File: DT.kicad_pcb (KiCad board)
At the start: 2 copper layers, 52 parts, among them SW1 SW_Push, SW10 SW_Push, SW11 SW_Push, SW12 SW_Push, SW2 SW_Push, SW3 SW_Push, SW4 SW_Push, SW5 SW_Push, SW6 SW_Push, SW7 SW_Push, SW8 SW_Push, SW9 SW_Push

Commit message: started wiring
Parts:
- removed REF**: DIP-28_W7.62mm, Package_DIP:DIP-28_W7.62mm
- removed REF**: Arduino_Nano, Module:Arduino_Nano
- added A1: Arduino_Nano_Every, Module:Arduino_Nano, F.Cu at (-260.8, 40.6)
- added R26: R, Resistor_THT:R_Axial_DIN0204_L3.6mm_D1.6mm_P5.08mm_Horizontal, F.Cu at (-241.6, 30.5)
- added U1: MCP23017_SP, Package_DIP:DIP-28_W7.62mm, F.Cu at (-253.8, -7.27)
- R1, R10, R11, R12, R13, R14, R15, R16, R17, R18, R19, R2, R20, R21, R22, R23, R24, R25, R3, R4, R5, R6, R7, R8, R9: footprint Resistor_THT:R_Axial_DIN0204_L3.6mm_D1.6mm_P1.90mm_Vertical -> Resistor_THT:R_Axial_DIN0204_L3.6mm_D1.6mm_P5.08mm_Horizontal
- moved R9 120.8 mm to (-365.2, 54.3)
- moved R1 119.9 mm to (-365.3, -5.25)
- moved R5 115.6 mm to (-365.0, 24.5)
- moved R25 96.7 mm to (-283.4, -43.7)
- moved R2 93.4 mm to (-335.6, -5.35)
- moved R10 90.4 mm to (-334.9, 54.2)
- moved R6 87.4 mm to (-335.5, 24.4)
- moved R21 81.1 mm to (-266.5, -26.9)
- moved R23 79.6 mm to (-266.5, -39.2)
- moved R24 78.1 mm to (-266.5, -34.4)
- moved R19 77.5 mm to (-266.5, -29.4)
- moved R17 73.9 mm to (-266.5, -31.9)
- moved R15 72.7 mm to (-266.5, -36.9)
- moved R3 69.4 mm to (-305.8, -5.14)
- moved R20 68.8 mm to (-266.5, -16.9)
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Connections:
- net +5V renamed Net-(A1-+5V)
- net GND renamed Net-(DS1-LED(-))
- R13 pad 1: Net-(A1-PadD22) -> Net-(U1-GPA3)
- R14 pad 1: Net-(A1-PadD23) -> Net-(U1-GPA2)
- R15 pad 1: Net-(A1-PadD24) -> Net-(U1-GPA1)
- R16 pad 1: Net-(A1-PadD25) -> Net-(U1-GPA0)
- R17 pad 1: Net-(A1-PadD26) -> Net-(U1-GPB7)
- R18 pad 1: Net-(A1-PadD32) -> Net-(U1-GPB1)
- R19 pad 1: Net-(A1-PadD30) -> Net-(U1-GPB3)
- R20 pad 1: Net-(A1-PadD29) -> Net-(U1-GPB4)
- R21 pad 1: Net-(A1-PadD28) -> Net-(U1-GPB5)
- R22 pad 1: Net-(A1-PadD27) -> Net-(U1-GPB6)
- R23 pad 1: Net-(A1-PadD33) -> Net-(U1-GPB0)
- R24 pad 1: Net-(A1-PadD31) -> Net-(U1-GPB2)
- SW1 pad 1: Net-(A1-PadD22) -> Net-(U1-GPB0)
- SW10 pad 1: Net-(A1-PadD31) -> Net-(U1-GPA1)
- SW11 pad 1: Net-(A1-PadD32) -> Net-(U1-GPA2)
- SW12 pad 1: Net-(A1-PadD33) -> Net-(U1-GPA3)
- SW2 pad 1: Net-(A1-PadD23) -> Net-(U1-GPB1)
- SW3 pad 1: Net-(A1-PadD24) -> Net-(U1-GPB2)
- SW4 pad 1: Net-(A1-PadD25) -> Net-(U1-GPB3)
- SW5 pad 1: Net-(A1-PadD26) -> Net-(U1-GPB4)
- SW6 pad 1: Net-(A1-PadD27) -> Net-(U1-GPB5)
- SW7 pad 1: Net-(A1-PadD28) -> Net-(U1-GPB6)
- SW8 pad 1: Net-(A1-PadD29) -> Net-(U1-GPB7)
- SW9 pad 1: Net-(A1-PadD30) -> Net-(U1-GPA0)
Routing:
- net Net-(DS1-LED(-)): track 0.00 -> 173.7 mm, vias 0 -> 1
- net Net-(A1-D5): track 0.00 -> 114.5 mm
- net Net-(A1-D7): track 0.00 -> 109.5 mm, vias 0 -> 1
- net Net-(A1-D4): track 0.00 -> 85.3 mm
- net Net-(A1-D3): track 0.00 -> 56.0 mm
- net Net-(A1-D6): track 0.00 -> 54.9 mm, vias 0 -> 1
- net Net-(A1-D2): track 0.00 -> 25.4 mm
- net Net-(D10-A): track 0.00 -> 5.56 mm
- net Net-(D8-A): track 0.00 -> 5.29 mm
- net Net-(D11-A): track 0.00 -> 5.17 mm
- net Net-(D7-A): track 0.00 -> 5.15 mm
- net Net-(D9-A): track 0.00 -> 5.04 mm
- net Net-(D12-A): track 0.00 -> 4.26 mm

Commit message: more wiring
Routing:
- net Net-(A1-D9): track 0.00 -> 161.4 mm, vias 0 -> 1
- net Net-(DS1-LED(-)): track 173.7 -> 334.2 mm, vias 1 -> 3
- net Net-(A1-A1): track 0.00 -> 156.4 mm, vias 0 -> 3
- net Net-(A1-A0): track 0.00 -> 132.3 mm, vias 0 -> 2
- net Net-(A1-A2): track 0.00 -> 124.1 mm, vias 0 -> 2
- net Net-(A1-D8): track 0.00 -> 117.6 mm, vias 0 -> 4
- net Net-(A1-D10): track 0.00 -> 88.7 mm, vias 0 -> 2
- net Net-(D5-A): track 0.00 -> 5.22 mm
- net Net-(D3-A): track 0.00 -> 5.00 mm
- net Net-(D6-A): track 0.00 -> 4.97 mm
- net Net-(D2-A): track 0.00 -> 4.90 mm
- net Net-(D4-A): track 0.00 -> 4.87 mm

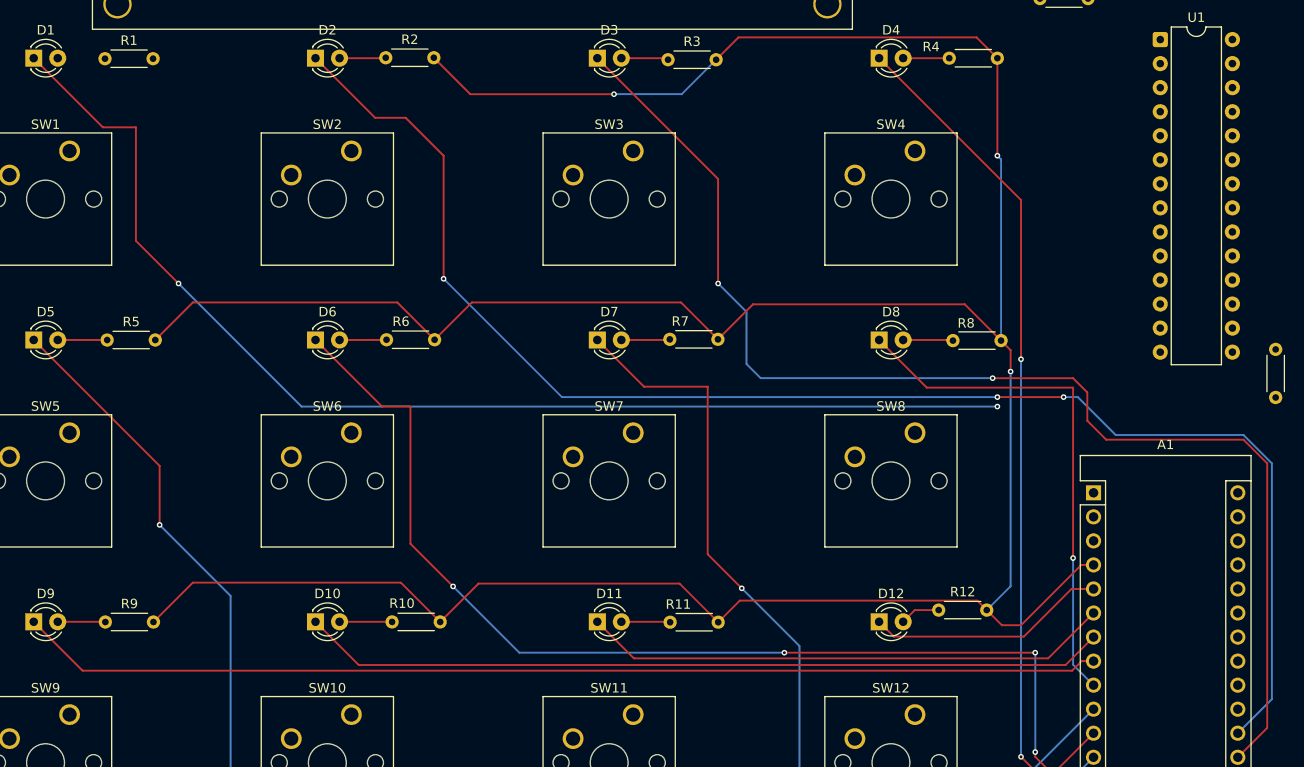
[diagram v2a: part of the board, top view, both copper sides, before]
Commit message: finished wiring LEDs
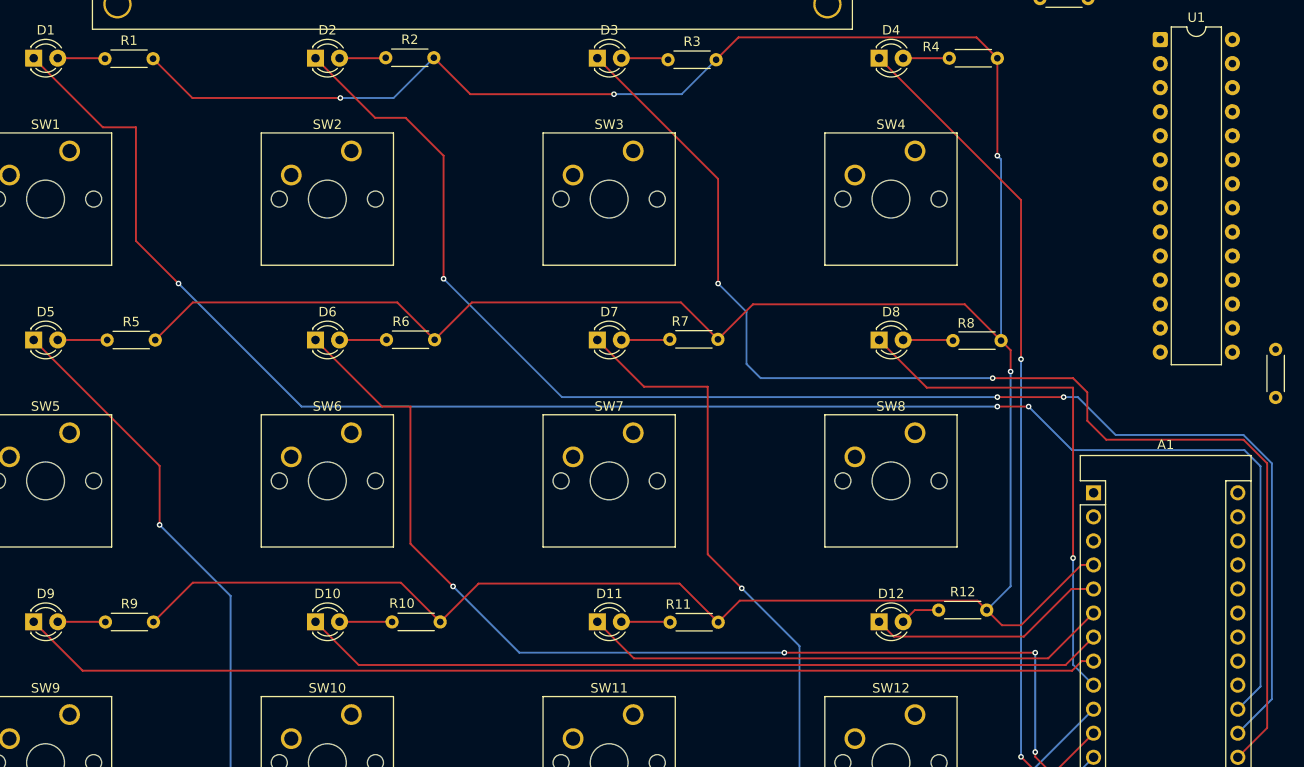
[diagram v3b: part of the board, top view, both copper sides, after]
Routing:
- net Net-(A1-A2): track 124.1 -> 181.2 mm, vias 2 -> 3
- net Net-(DS1-LED(-)): track 334.2 -> 367.4 mm, vias 3 -> 4
- net Net-(D1-A): track 0.00 -> 5.01 mm
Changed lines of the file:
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@@
+	)
+	(segment
+		(start -370.262 -5.305)
+		(end -365.325 -5.305)
+		(width 0.2)
+		(layer "F.Cu")
+		(net 1)
+	)
+	(segment
+		(start -365.325 -5.305)
+		(end -365.27 -5.25)
+		(width 0.2)
+		(layer "F.Cu")
+		(net 1)
 	)
 	(segment
@@
 	)
 	(segment
+		(start -271 31.5)
+		(end -267.7 31.5)
+		(width 0.2)
+		(layer "F.Cu")
+		(net 22)
+	)
+	(segment
 		(start -362 14)
 		(end -357.5 18.5)
@@
 	)
 	(via
+		(at -267.7 31.5)
+		(size 0.6)
+		(drill 0.3)
+		(layers "F.Cu" "B.Cu")
+		(net 22)
+	)
+	(via
 		(at -357.5 18.5)
 		(size 0.6)
@@
 		(drill 0.3)
 		(layers "F.Cu" "B.Cu")
+		(net 22)
+	)
+	(segment
+		(start -267.7 31.5)
+		(end -263.1 36.1)
+		(width 0.2)
+		(layer "B.Cu")
 		(net 22)
 	)
@@
 	)
 	(segment
+		(start -243.2 61.07)
+		(end -245.6 63.47)
+		(width 0.2)
+		(layer "B.Cu")
+		(net 22)
+	)
+	(segment
+		(start -243.2 37.8)
+		(end -243.2 61.07)
+		(width 0.2)
+		(layer "B.Cu")
+		(net 22)
+	)
+	(segment
+		(start -244.9 36.1)
+		(end -243.2 37.8)
+		(width 0.2)
+		(layer "B.Cu")
+		(net 22)
+	)
+	(segment
+		(start -263.1 36.1)
+		(end -244.9 36.1)
+		(width 0.2)
+		(layer "B.Cu")
+		(net 22)
+	)
+	(segment
 		(start -344.5 31.5)
 		(end -271 31.5)
@@
 	)
 	(segment
+		(start -360.19 -5.25)
+		(end -356.04 -1.1)
+		(width 0.2)
+		(layer "F.Cu")
+		(net 38)
+	)
+	(segment
+		(start -356.04 -1.1)
+		(end -340.4 -1.1)
+		(width 0.2)
+		(layer "F.Cu")
+		(net 38)
+	)
+	(segment
 		(start -304.57 50.2)
 		(end -300.49 54.28)
@@
 	)
 	(via
+		(at -340.4 -1.1)
+		(size 0.6)
+		(drill 0.3)
+		(layers "F.Cu" "B.Cu")
+		(net 38)
+	)
+	(via
 		(at -311.5 -1.5)
 		(size 0.6)
@@
 	)
 	(segment
+		(start -340.4 -1.1)
+		(end -334.78 -1.1)
+		(width 0.2)
+		(layer "B.Cu")
+		(net 38)
+	)
+	(segment
 		(start -271 5)
 		(end -270.61 5.39)
@@
 		(width 0.2)
 		(layer "B.Cu")
+		(net 38)
+	)
+	(segment
+		(start -334.78 -1.1)
+		(end -330.53 -5.35)
+		(width 0.2)
+		(layer "B.Cu")

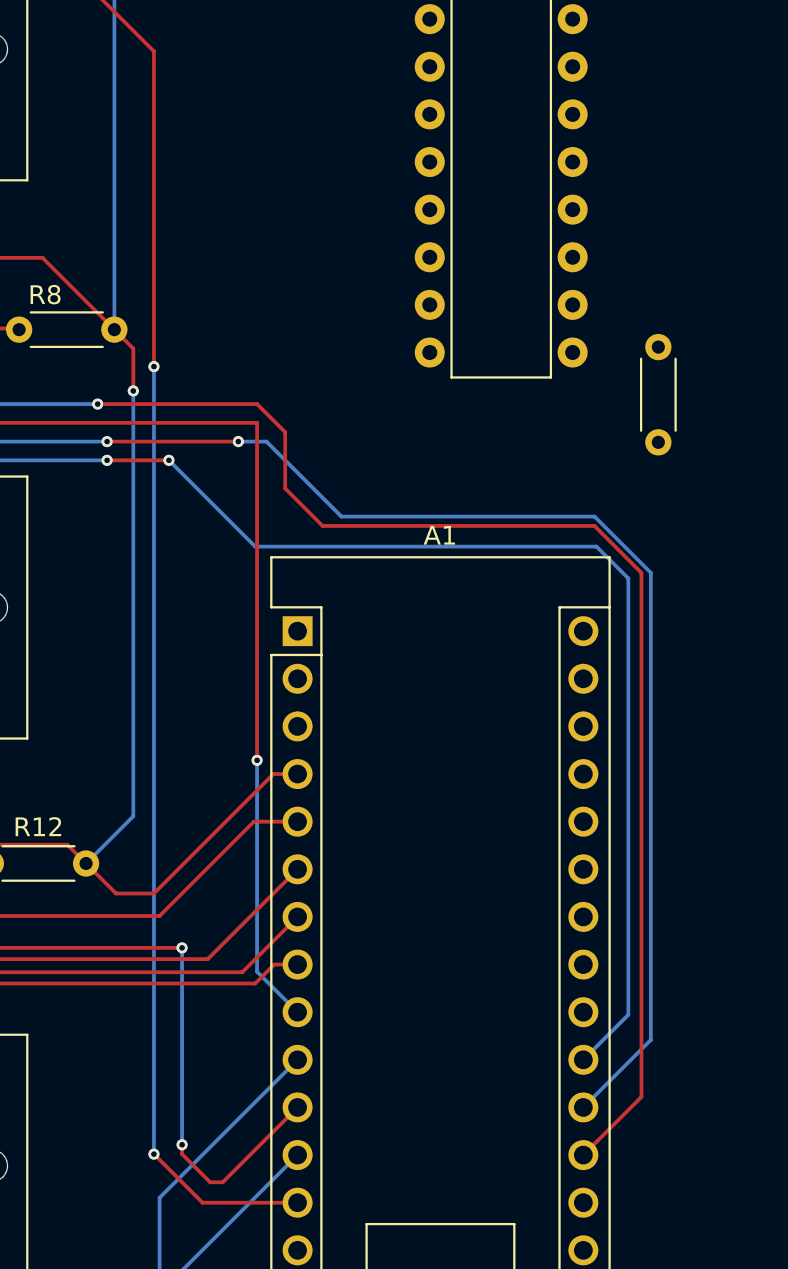
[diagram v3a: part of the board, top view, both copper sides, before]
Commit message: wired up mcp
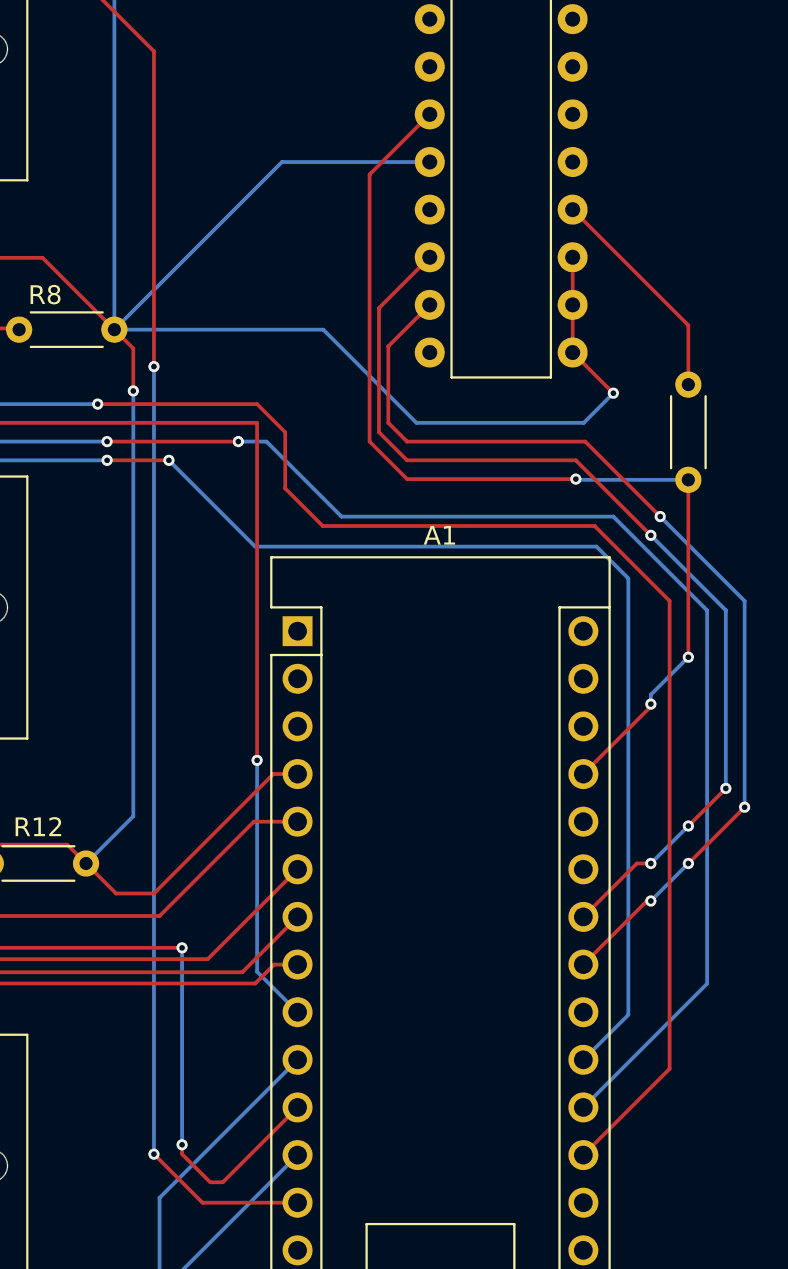
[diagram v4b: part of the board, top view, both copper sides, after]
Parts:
- moved R26 2.56 mm to (-240.0, 32.5)
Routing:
- net Net-(DS1-LED(-)): track 367.4 -> 425.4 mm, vias 4 -> 5
- net Net-(A1-+5V): track 0.00 -> 54.6 mm, vias 0 -> 3
- net Net-(A1-SDA/A4): track 0.00 -> 53.2 mm, vias 0 -> 4
- net Net-(A1-SCL/A5): track 0.00 -> 52.8 mm, vias 0 -> 4
- net Net-(U1-~{RESET}): track 0.00 -> 11.9 mm
- net Net-(A1-A1): track 156.4 -> 159.4 mm
- net Net-(A1-A0): track 132.3 -> 133.5 mm

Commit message: wirws
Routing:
- net Net-(U1-GPA0): track 0.00 -> 186.3 mm, vias 0 -> 3
- net Net-(U1-GPA1): track 0.00 -> 154.2 mm, vias 0 -> 3
- net Net-(U1-GPB4): track 0.00 -> 137.1 mm, vias 0 -> 4
- net Net-(U1-GPB0): track 0.00 -> 120.7 mm
- net Net-(U1-GPB5): track 0.00 -> 115.3 mm, vias 0 -> 3
- net Net-(U1-GPB1): track 0.00 -> 91.6 mm
- net Net-(U1-GPB6): track 0.00 -> 76.4 mm, vias 0 -> 5
- net Net-(U1-GPB2): track 0.00 -> 59.9 mm
- net Net-(U1-GPB7): track 0.00 -> 45.2 mm, vias 0 -> 1
- net Net-(U1-GPB3): track 0.00 -> 29.2 mm

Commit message: almost finished switches
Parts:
- moved R13 14.2 mm to (-252.3, -14.7)
- moved R14 14.2 mm to (-252.3, -11.9)
- moved R15 14.2 mm to (-252.3, -37.2)
- moved R16 14.2 mm to (-252.3, -22.2)
- moved R17 14.2 mm to (-252.3, -32.2)
- moved R18 14.2 mm to (-252.3, -19.8)
- moved R19 14.2 mm to (-252.3, -29.8)
- moved R20 14.2 mm to (-252.3, -17.2)
- moved R21 14.2 mm to (-252.3, -27.2)
- moved R22 14.2 mm to (-252.3, -24.8)
- moved R23 14.2 mm to (-252.3, -39.6)
- moved R24 14.2 mm to (-252.3, -34.8)
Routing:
- net Net-(A1-+5V): track 54.6 -> 491.7 mm, vias 3 -> 12
- net Net-(U1-GPA2): track 0.00 -> 165.4 mm, vias 0 -> 1
- net Net-(U1-GPA3): track 0.00 -> 139.5 mm, vias 0 -> 1
- net Net-(DS1-LED(-)): track 425.4 -> 532.2 mm, vias 5 -> 9
- net Net-(U1-GPB5): track 115.3 -> 214.9 mm, vias 3 -> 6
- net Net-(U1-GPB0): track 120.7 -> 217.3 mm
- net Net-(U1-GPB2): track 59.9 -> 156.0 mm, vias 0 -> 1
- net Net-(U1-GPB3): track 29.2 -> 122.5 mm, vias 0 -> 1
- net Net-(U1-GPB4): track 137.1 -> 189.2 mm, vias 4 -> 10
- net Net-(U1-GPB1): track 91.6 -> 112.8 mm, vias 0 -> 1
- net Net-(U1-GPB6): track 76.4 -> 93.9 mm, vias 5 -> 7

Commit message: finished
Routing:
- net Net-(A1-+5V): track 491.7 -> 695.6 mm, vias 12 -> 17
- net Net-(A1-A6): track 0.00 -> 192.4 mm, vias 0 -> 4
- net Net-(A1-A7): track 0.00 -> 186.2 mm, vias 0 -> 4
- net Net-(DS1-RS): track 0.00 -> 162.9 mm, vias 0 -> 1
- net Net-(DS1-E): track 0.00 -> 155.8 mm, vias 0 -> 1
- net Net-(DS1-LED(-)): track 532.2 -> 683.5 mm
- net Net-(DS1-D4): track 0.00 -> 141.2 mm, vias 0 -> 1
- net Net-(DS1-D5): track 0.00 -> 136.4 mm, vias 0 -> 1
- net Net-(U1-GPA1): track 154.2 -> 281.9 mm, vias 3 -> 9
- net Net-(U1-GPB7): track 45.2 -> 154.2 mm, vias 1 -> 6
- net Net-(U1-GPA0): track 186.3 -> 273.8 mm, vias 3 -> 9
- net Net-(U1-GPB6): track 93.9 -> 172.5 mm
- net Net-(U1-GPA3): track 139.5 -> 181.5 mm
- net Net-(DS1-LED(+)): track 0.00 -> 40.2 mm
- net Net-(U1-GPA2): track 165.4 -> 202.3 mm, vias 1 -> 3
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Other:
- board outline added: 154 x 137.8 mm
